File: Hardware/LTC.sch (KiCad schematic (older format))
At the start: 85 parts, among them J10 Conn_01x01_Female, J11 Conn_01x01_Female, J12 Conn_01x01_Female, J14 Conn_01x02_Male, J15 Conn_01x02_Male, J16 Conn_01x02_Male, J6 Conn_01x01_Female, J7 Conn_01x01_Female, J8 Conn_01x01_Female, J9 Conn_01x01_Female, Q2 Q_NMOS_GSD, Q3 Q_NMOS_GSD, Q4 Q_NMOS_GSD, Q5 Q_NMOS_GSD, Q6 Q_NMOS_GSD, Q7 Q_NMOS_GSD, Q9 Q_NPN_BCE

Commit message: PCB changes + MXCube
-gitignore added to the Hardware and Software sections
-Changed power section wiring on PCB
-MXCube file created as a beginning of Software section
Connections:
- net labels added: +24V
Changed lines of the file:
@@
 Wire Wire Line
 	4450 3000 4900 3000
+$Comp
+L power:+24V #PWR?
+U 1 1 60770816
+P 3050 2250
+AR Path="/60770816" Ref="#PWR?"  Part="1"
+AR Path="/5FF86554/60770816" Ref="#PWR0106"  Part="1"
+F 0 "#PWR0106" H 3050 2100 50  0001 C CNN
+F 1 "+24V" H 3065 2423 50  0000 C CNN
+F 2 "" H 3050 2250 50  0001 C CNN
+F 3 "" H 3050 2250 50  0001 C CNN
+	1    3050 2250
+	1    0    0    -1
+$EndComp
 $EndSCHEMATC

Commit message: J13, J14, J15 footprint change
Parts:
- J14, J15, J16: footprint Connector_PinHeader_2.54mm:PinHeader_1x02_P2.54mm_Vertical -> Jumper:SolderJumper-2_P1.3mm_Open_RoundedPad1.0x1.5mm
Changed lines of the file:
@@
 EESchema Schematic File Version 4
+LIBS:bmsLV-cache
 EELAYER 30 0
 EELAYER END
@@
 F 0 "J16" V 5362 1994 50  0000 L CNN
 F 1 "Conn_01x02_Male" V 5453 1994 50  0000 L CNN
-F 2 "Connector_PinHeader_2.54mm:PinHeader_1x02_P2.54mm_Vertical" H 5300 1950 50  0001 C CNN
+F 2 "Jumper:SolderJumper-2_P1.3mm_Open_RoundedPad1.0x1.5mm" H 5300 1950 50  0001 C CNN
 F 3 "~" H 5300 1950 50  0001 C CNN
 	1    5300 1950
@@
 F 0 "J15" H 4608 2731 50  0000 C CNN
 F 1 "Conn_01x02_Male" H 4608 2640 50  0000 C CNN
-F 2 "Connector_PinHeader_2.54mm:PinHeader_1x02_P2.54mm_Vertical" H 4500 2550 50  0001 C CNN
+F 2 "Jumper:SolderJumper-2_P1.3mm_Open_RoundedPad1.0x1.5mm" H 4500 2550 50  0001 C CNN
 F 3 "~" H 4500 2550 50  0001 C CNN
 	1    4500 2550
@@
 F 0 "J14" H 4358 3081 50  0000 C CNN
 F 1 "Conn_01x02_Male" H 4358 2990 50  0000 C CNN
-F 2 "Connector_PinHeader_2.54mm:PinHeader_1x02_P2.54mm_Vertical" H 4250 2900 50  0001 C CNN
+F 2 "Jumper:SolderJumper-2_P1.3mm_Open_RoundedPad1.0x1.5mm" H 4250 2900 50  0001 C CNN
 F 3 "~" H 4250 2900 50  0001 C CNN
 	1    4250 2900

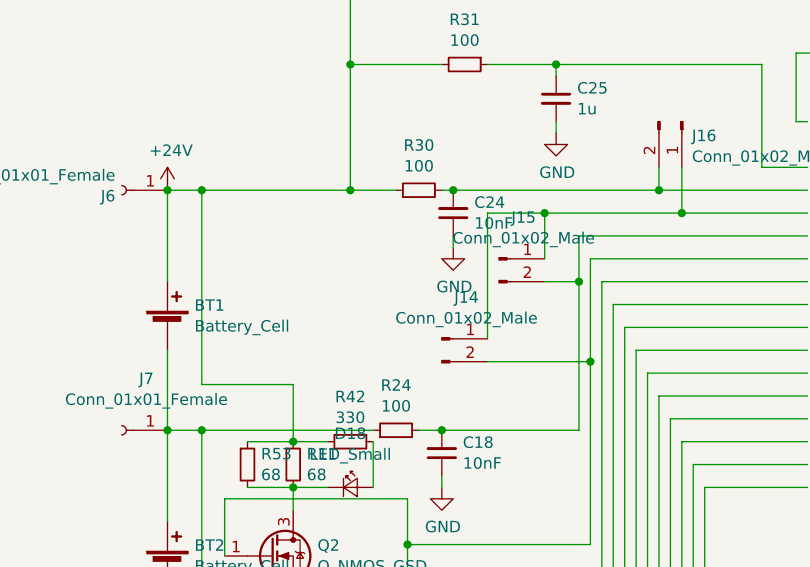
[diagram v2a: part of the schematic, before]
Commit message: Dash Led and jumpers
-output to Dash Led created
-added another jumper (J17) to ground
-J14, J15, J16 jumper position changed
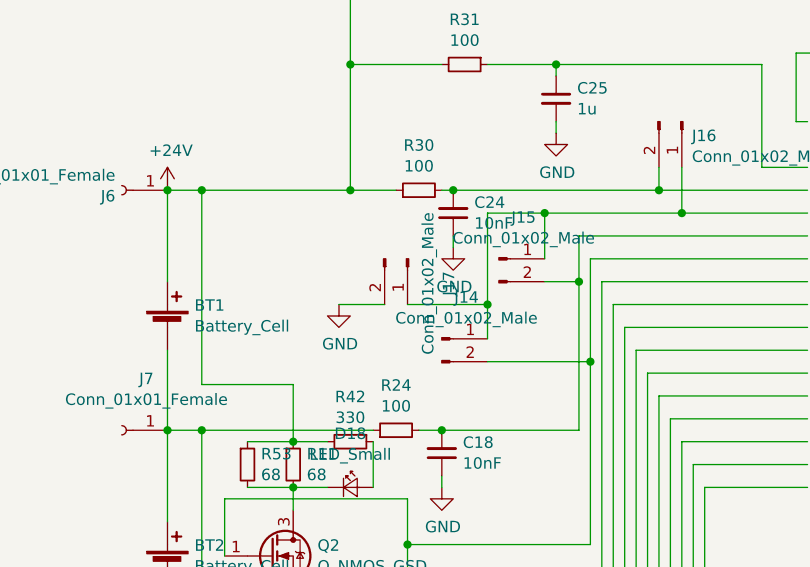
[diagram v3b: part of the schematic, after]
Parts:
- added J17: Conn_01x02_Male, Jumper:SolderJumper-2_P1.3mm_Open_RoundedPad1.0x1.5mm, symbol Connector:Conn_01x02_Male
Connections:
- wire segments 292 -> 295
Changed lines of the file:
@@
 EESchema Schematic File Version 4
-LIBS:bmsLV-cache
 EELAYER 30 0
 EELAYER END
@@
 	4900 3000 4900 2550
 Wire Wire Line
-	4450 2350 4450 2900
+	4450 2350 4450 2750
 Wire Wire Line
 	4450 3000 4900 3000
@@
 	1    0    0    -1
 $EndComp
+Wire Wire Line
+	4450 2750 4100 2750
+Connection ~ 4450 2750
+Wire Wire Line
+	4450 2750 4450 2900
+$Comp
+L Connector:Conn_01x02_Male J17
+U 1 1 6089DF71
+P 4100 2550
+F 0 "J17" H 4208 2731 50  0000 C CNN
+F 1 "Conn_01x02_Male" H 4208 2640 50  0000 C CNN
+F 2 "Jumper:SolderJumper-2_P1.3mm_Open_RoundedPad1.0x1.5mm" H 4100 2550 50  0001 C CNN
+F 3 "~" H 4100 2550 50  0001 C CNN
+	1    4100 2550
+	0    1    1    0
+$EndComp
+Wire Wire Line
+	4000 2750 3800 2750
+$Comp
+L power:GND #PWR0107
+U 1 1 608CD223
+P 3800 2750
+F 0 "#PWR0107" H 3800 2500 50  0001 C CNN
+F 1 "GND" H 3805 2577 50  0000 C CNN
+F 2 "" H 3800 2750 50  0001 C CNN
+F 3 "" H 3800 2750 50  0001 C CNN
+	1    3800 2750
+	1    0    0    -1
+$EndComp

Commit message: STM changed
Due to the lack of processors on market, we decided to change STM32F103C8T6 for STM32F4P5RET. So the schematic and PCB is significantly changed in this area.
Furthermore, the library and footprint to new processor was added.
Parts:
- removed LTC1: LTC6810-1, Package_SO:SSOP-44_5.3x12.8mm_P0.5mm, symbol LTC6810-1:LTC6810-1-LTC6810-1
- added LTC68101: LTC6810-1-LTC6810-1, footprints:LTC6810, symbol LTC6810-1:LTC6810-1-LTC6810-1
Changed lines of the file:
@@
 MOSI
-Wire Wire Line
-	5850 1950 5800 1950
-Wire Wire Line
-	5800 1950 5800 1650
-Wire Wire Line
-	5800 1650 6450 1650
-Wire Wire Line
-	7100 1650 7100 1950
-Wire Wire Line
-	7100 2050 7050 2050
-Wire Wire Line
-	7100 1950 7050 1950
-Connection ~ 7100 1950
-Wire Wire Line
-	7100 1950 7100 2050
-Connection ~ 6450 1650
-Wire Wire Line
-	6450 1650 7100 1650
-$Comp
-L power:GND #PWR044
-U 1 1 604A2D56
-P 6550 1500
-F 0 "#PWR044" H 6550 1250 50  0001 C CNN
-F 1 "GND" H 6555 1327 50  0000 C CNN
-F 2 "" H 6550 1500 50  0001 C CNN
-F 3 "" H 6550 1500 50  0001 C CNN
-	1    6550 1500
-	1    0    0    -1
-$EndComp
 Wire Wire Line
 	3850 2250 3850 1700
@@
 	8750 2600 8900 2600
 $Comp
-L LTC6810-1:LTC6810-1-LTC6810-1 LTC?
-U 1 1 5FF8D74A
-P 7350 4100
-AR Path="/5FF8D74A" Ref="LTC?"  Part="1"
-AR Path="/5FF86554/5FF8D74A" Ref="LTC1"  Part="1"
-F 0 "LTC1" H 6450 6475 50  0000 C CNN
-F 1 "LTC6810-1" H 6450 6384 50  0000 C CNN
-F 2 "Package_SO:SSOP-44_5.3x12.8mm_P0.5mm" H 6200 5150 50  0001 C CNN
-F 3 "" H 6200 5150 50  0001 C CNN
-	1    7350 4100
-	1    0    0    -1
-$EndComp
-$Comp
 L power:GND #PWR047
 U 1 1 605F8879
@@
 	1    0    0    -1
 $EndComp
-Wire Wire Line
-	6550 1500 6450 1500
-Wire Wire Line
-	6450 1500 6450 1650
 Connection ~ 3200 8550
 Wire Wire Line
@@
 	1    0    0    -1
 $EndComp
+$Comp
+L LTC6810-1:LTC6810-1-LTC6810-1 LTC68101
+U 1 1 608C9646
+P 7350 4100
+F 0 "LTC68101" H 6450 6475 50  0000 C CNN
+F 1 "LTC6810-1-LTC6810-1" H 6450 6384 50  0000 C CNN
+F 2 "footprints:LTC6810" H 6200 5150 50  0001 C CNN
+F 3 "" H 6200 5150 50  0001 C CNN
+	1    7350 4100
+	1    0    0    -1
+$EndComp
+Wire Wire Line
+	5800 1650 6450 1650
+Connection ~ 6450 1650
+Wire Wire Line
+	6450 1650 7100 1650
+Wire Wire Line
+	6450 1500 6450 1650
+Wire Wire Line
+	6550 1500 6450 1500
+$Comp
+L power:GND #PWR044
+U 1 1 604A2D56
+P 6550 1500
+F 0 "#PWR044" H 6550 1250 50  0001 C CNN
+F 1 "GND" H 6555 1327 50  0000 C CNN
+F 2 "" H 6550 1500 50  0001 C CNN
+F 3 "" H 6550 1500 50  0001 C CNN
+	1    6550 1500
+	1    0    0    -1
+$EndComp
+Wire Wire Line
+	7100 1950 7100 2050
+Connection ~ 7100 1950
+Wire Wire Line
+	7100 1950 7050 1950
+Wire Wire Line
+	7100 2050 7050 2050
+Wire Wire Line
+	7100 1650 7100 1950
+Wire Wire Line
+	5800 1950 5800 1650
+Wire Wire Line
+	5850 1950 5800 1950
 $EndSCHEMATC

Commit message: Some changes
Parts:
- LTC68101: symbol LTC6810-1:LTC6810-1-LTC6810-1 -> bmsLV-rescue:LTC6810-1-LTC6810-1-LTC6810-1
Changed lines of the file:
@@
 EESchema Schematic File Version 4
-EELAYER 30 0
+LIBS:bmsLV-cache
+EELAYER 29 0
 EELAYER END
 $Descr A3 16535 11693
@@
 $EndComp
 $Comp
-L LTC6810-1:LTC6810-1-LTC6810-1 LTC68101
+L bmsLV-rescue:LTC6810-1-LTC6810-1-LTC6810-1 LTC68101
 U 1 1 608C9646
 P 7350 4100

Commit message: Software update 3
Current sensor added to PCB (through wires)
Current sensor handling added
Cell balance working! (HUGE PART OF UPDATE)
CheckError function modified (a lot of more error added)
Serial print function added (not tested)
+ some cosmetic changes
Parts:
- removed J14, J15, J16, J17: Conn_01x02_Male, Jumper:SolderJumper-2_P1.3mm_Open_RoundedPad1.0x1.5mm, symbol Connector:Conn_01x02_Male
- BT1, BT2, BT3, BT4, BT5, BT6: symbol Device:Battery_Cell -> bmsLV-rescue:Battery_Cell-Device
- C18, C19, C20, C21, C22, C23, C24, C25, C26, C27, C28, C29: symbol Device:C_Small -> bmsLV-rescue:C_Small-Device
- D10, D11, D12, D13, D14, D15: symbol Device:D_Zener_Small -> bmsLV-rescue:D_Zener_Small-Device
- D18, D19, D20, D21, D22, D23: symbol Device:LED_Small -> bmsLV-rescue:LED_Small-Device
- J10, J11, J12, J6, J7, J8, J9: symbol Connector:Conn_01x01_Female -> bmsLV-rescue:Conn_01x01_Female-Connector
- Q2, Q3, Q4, Q5, Q6, Q7: symbol Device:Q_NMOS_GSD -> bmsLV-rescue:Q_NMOS_GSD-Device
- Q9: symbol Device:Q_NPN_BCE -> bmsLV-rescue:Q_NPN_BCE-Device
- R11, R12, R13, R14, R15, R16, R18, R19, R20, R21, R22, R23, R24, R25, R26, R27, R28, R29, R30, R31, R32, R42, R43, R44, R45, R46, R47, R48, R49, R50, R51, R53, R54, R55, R56, R57, R58: symbol Device:R_Small -> bmsLV-rescue:R_Small-Device
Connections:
- net at C24.2, LTC68101.4 (C6), R30.2: now also LTC68101.5 (S6)
